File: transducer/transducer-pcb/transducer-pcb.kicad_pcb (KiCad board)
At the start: 4 copper layers, 48 x 60 mm, 14 parts, among them J1 Load Cell, J2 Sheild, J3 RJ45, J4 AMP RIGHT, J5 AMP LEFT, J6 NANO UR, J7 NANO LR, J8 NANO UL, J9 NANO LL

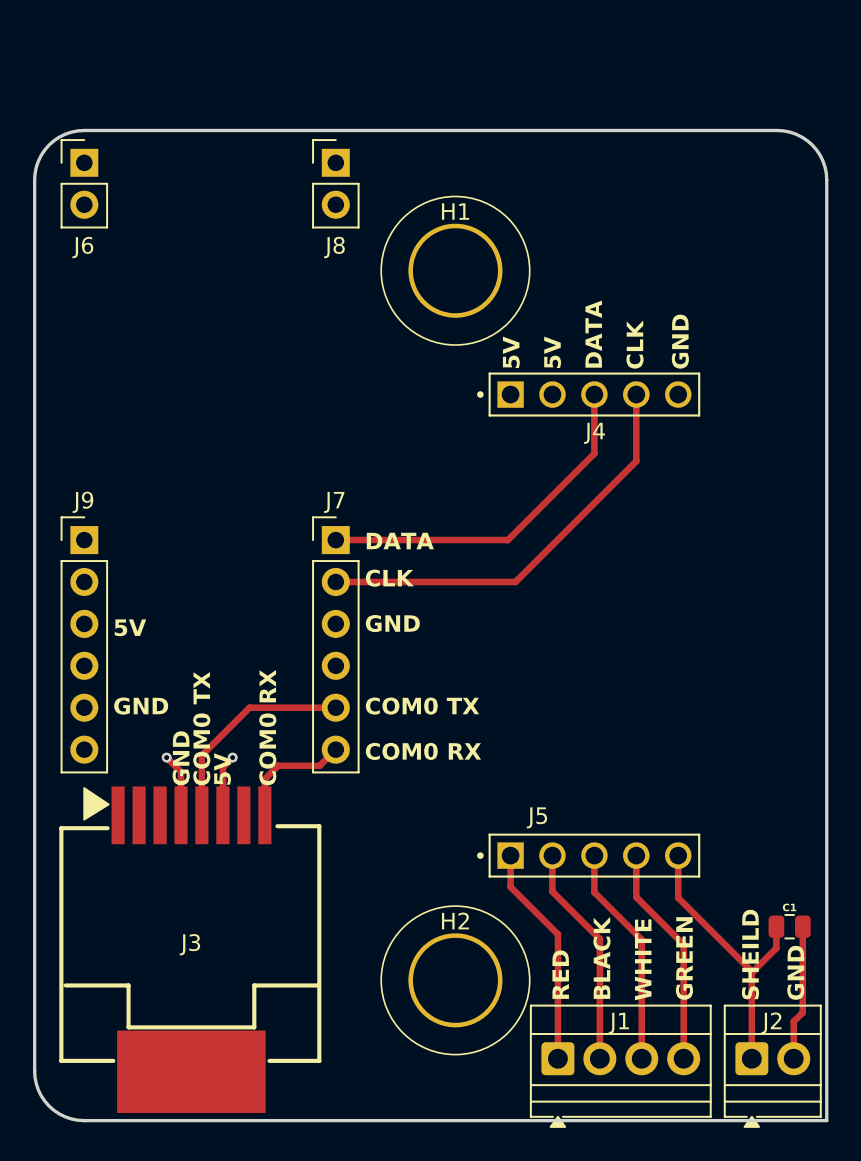
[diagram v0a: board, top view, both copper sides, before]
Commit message: Rev B PCBA and move arduino file to folder
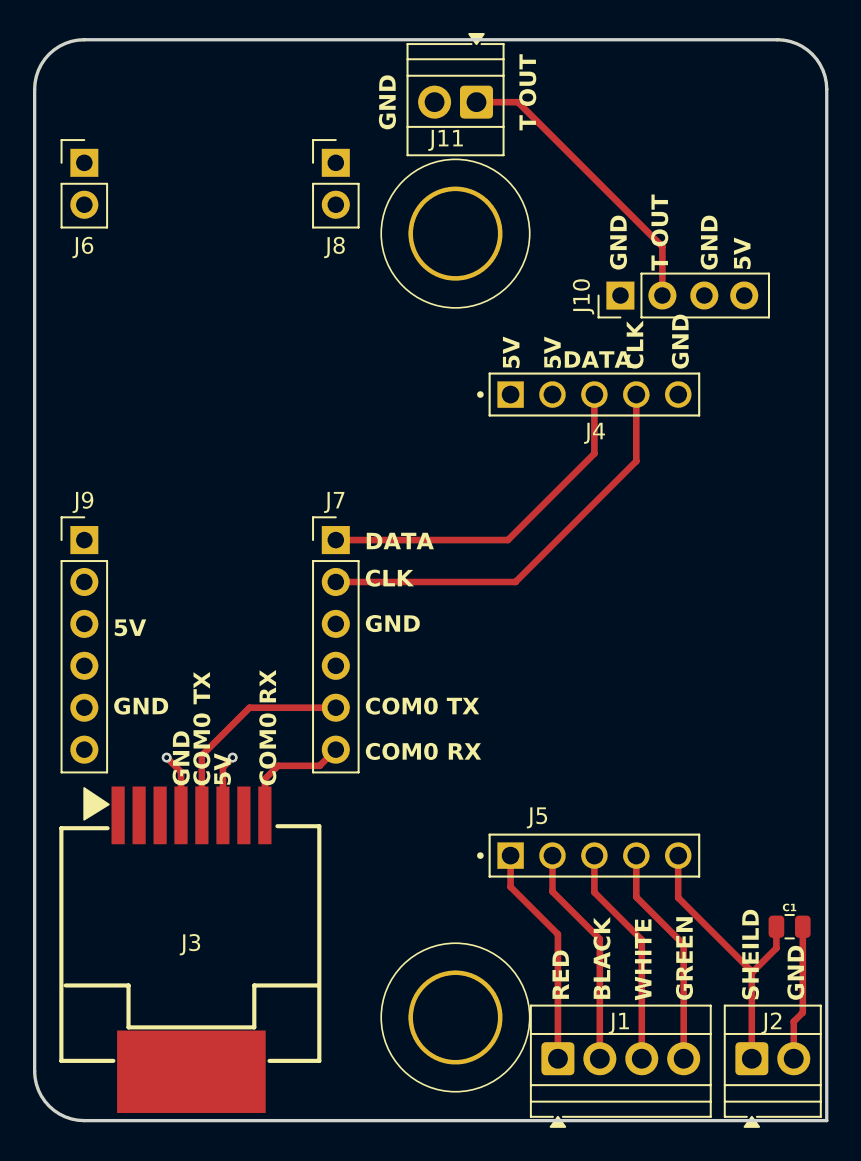
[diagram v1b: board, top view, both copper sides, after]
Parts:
- added J10: Thermocouple Board, BR_Connectors:Pin_Header_1x4_2.54mm_Vertical, F.Cu at (282.5, 100.0)
- added J11: Thermocouple Out, BR_Connectors:KF128-2.54-2P, F.Cu at (273.8, 88.3)
- moved H1 2.25 mm to (272.5, 96.2)
- moved H2 2.25 mm to (272.5, 143.8)
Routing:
- net /T_OUT: track 0.00 -> 17.9 mm
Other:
- board size 48 x 60 mm -> 48 x 65.5 mm
- board text added: "LOAD CELL AND THERMOCOUPLE CONDITIONING BOARD"
- board text added: "T OUT"
